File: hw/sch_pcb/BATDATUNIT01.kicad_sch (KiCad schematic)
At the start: 116 parts, among them IC1 MAX14502AETL+, J1 USBC_USB4105-GF-A, J22 HEADER_2x03, J4 46436-9327, J9 SD_Card-FPS009-4200-0, Q1 BC817-25, Q2 BC817-25, Q3 BC817-25, Q4 BC817-25, SW3 KMT031, SW3 SKRTLAE010, SW4 KMT031, SW4 SKRTLAE010, U10 ATMEGA1284P-AU, U11 PCF85263A, U11 TCA4307, U2 USBLC6-2SC6, U3 FT260Q-T, U4 PCA9541ABS/01, U6 AT24CS64-SSHM, U6 SHT35-DIS, U7 TMUX1574DYYR, Y1 19.2 MHz, Y1 8 MHz, Y2 ABS07-120-32.768KHZ-T

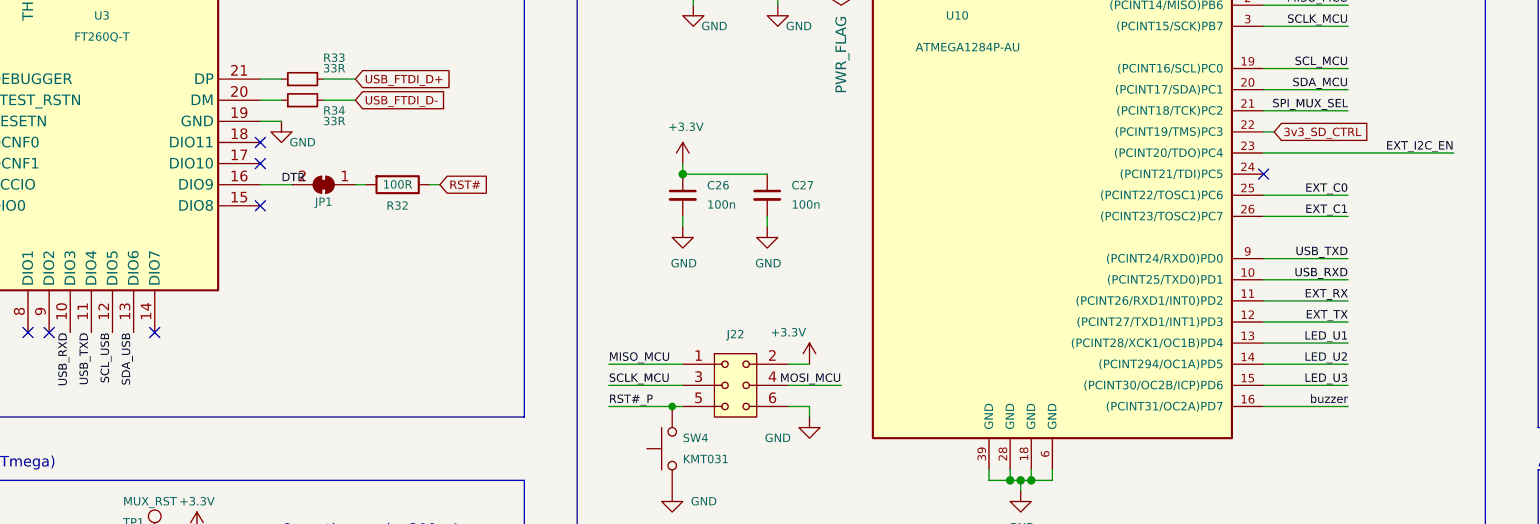
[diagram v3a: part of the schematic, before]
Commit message: add USB detect from FTDI to MCU
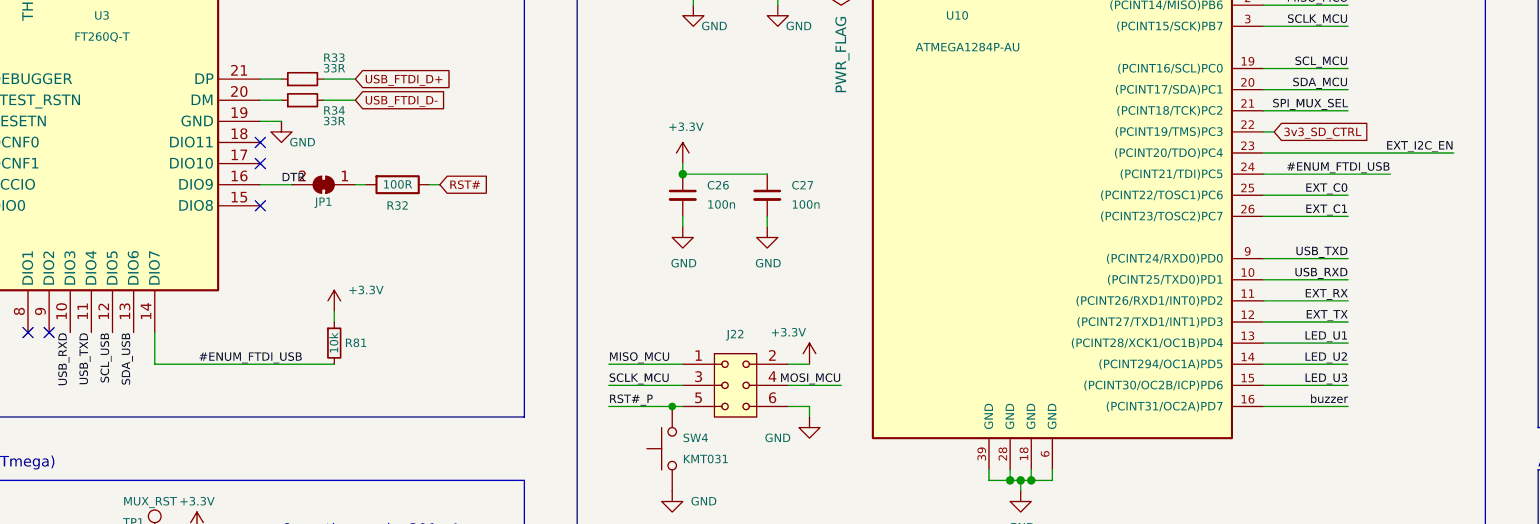
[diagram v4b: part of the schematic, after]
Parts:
- added R81: 10k, Resistor_SMD:R_0805_2012Metric, symbol Device:R_Small
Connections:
- net +3.3V: now also R81.1
- net #ENUM_FTDI_USB: now reaches U10.24 ((PCINT21/TDI)PC5)
- net #ENUM_FTDI_USB: now also U3.14 (DIO7), R81.2
- no-connect marks 38 -> 36
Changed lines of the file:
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@@
   (no_connect (at 151.13 243.84))
   (no_connect (at 355.6 196.85))
-  (no_connect (at 304.8 184.15))
   (no_connect (at 60.96 163.83))
   (no_connect (at 318.77 52.07))
   (no_connect (at 304.8 135.89))
   (no_connect (at 40.64 135.89))
-  (no_connect (at 171.45 203.2))
   (no_connect (at 378.46 68.58))
   (no_connect (at 151.13 254))
@@
     (stroke (width 0) (type default))
   )
+  (wire (pts (xy 304.8 184.15) (xy 320.04 184.15))
+    (stroke (width 0) (type default))
+  )
   (wire (pts (xy 109.22 49.53) (xy 109.22 48.26))
     (stroke (width 0) (type default))
@@
     (stroke (width 0) (type default))
   )
+  (wire (pts (xy 193.04 200.66) (xy 193.04 201.93))
+    (stroke (width 0) (type default))
+  )
   (wire (pts (xy 233.68 146.05) (xy 237.49 146.05))
     (stroke (width 0) (type default))
@@
     (stroke (width 0) (type default))
   )
+  (wire (pts (xy 171.45 207.01) (xy 193.04 207.01))
+    (stroke (width 0) (type default))
+  )
   (wire (pts (xy 368.3 232.41) (xy 368.3 233.68))
     (stroke (width 0) (type default))
@@
     (stroke (width 0) (type default))
   )
+  (wire (pts (xy 171.45 207.01) (xy 171.45 203.2))
+    (stroke (width 0) (type default))
+  )
   (wire (pts (xy 274.32 219.71) (xy 274.32 220.98))
     (stroke (width 0) (type solid))
@@
     (effects (font (size 1 1)) (justify left bottom))
   )
+  (label "#ENUM_FTDI_USB" (at 189.23 207.01 180) (fields_autoplaced)
+    (effects (font (size 1 1)) (justify right bottom))
+  )
   (label "RST#_P" (at 226.06 212.09 0) (fields_autoplaced)
     (effects (font (size 1 1)) (justify left bottom))
@@
     (effects (font (size 1 1)) (justify right bottom))
   )
+  (label "#ENUM_FTDI_USB" (at 320.04 184.15 180) (fields_autoplaced)
+    (effects (font (size 1 1)) (justify right bottom))
+  )
   (label "LED_U3" (at 128.27 104.14 0) (fields_autoplaced)
     (effects (font (size 1 1)) (justify left bottom))
@@
     )
   )
+  (symbol (lib_id "Device:R_Small") (at 193.04 204.47 0) (unit 1)
+    (in_bom yes) (on_board yes) (dnp no)
+    (property "Reference" "R81" (at 194.31 204.47 0)
+      (effects (font (size 1 1)) (justify left))
+    )
+    (property "Value" "10k" (at 193.04 205.74 90)
+      (effects (font (size 1 1)) (justify left))
+    )
+    (property "Footprint" "Resistor_SMD:R_0805_2012Metric" (at 193.04 204.47 0)
+      (effects (font (size 1 1)) hide)
+    )
+    (property "Datasheet" "~" (at 193.04 204.47 0)
+      (effects (font (size 1 1)) hide)
+    )
+    (property "UST_ID" "" (at 193.04 204.47 0)
+      (effects (font (size 1 1)) hide)
+    )
+    (pin "1")
+    (pin "2")
+    (instances
+      (project "BATDATUNIT01"
+        (path "/cca3030a-cb35-4155-89c2-3a41e5a0afad"
+          (reference "R81") (unit 1)
+        )
+      )
+    )
+  )
   (symbol (lib_id "Mechanical:Fiducial") (at 40.64 271.78 0) (unit 1)
     (in_bom no) (on_board yes) (dnp no) (fields_autoplaced)
@@
         )
       )
+    )
+  )
+  (symbol (lib_id "power:+3.3V") (at 193.04 200.66 0) (unit 1)
+    (in_bom yes) (on_board yes) (dnp no)
+    (property "Reference" "#PWR?" (at 193.04 204.47 0)
+      (effects (font (size 1 1)) hide)
+    )
+    (property "Value" "+3.3V" (at 196.85 198.12 0)
+      (effects (font (size 1 1)))
+    )
+    (property "Footprint" "" (at 193.04 200.66 0)
+      (effects (font (size 1 1)) hide)
+    )
+    (property "Datasheet" "" (at 193.04 200.66 0)
+      (effects (font (size 1 1)) hide)
+    )
+    (pin "1")
+    (instances
+      (project "Peripherals"
+        (path "/5251a3af-ca7f-447d-b796-a6d47f48d23f"
+          (reference "#PWR?") (unit 1)
+        )
+      )
+      (project "BATDATUNIT01"
+        (path "/cca3030a-cb35-4155-89c2-3a41e5a0afad"
+          (reference "#PWR01") (unit 1)
+        )
+      )
+      (project "DATALOGGER02"
+        (path "/d5fa3405-b56f-43e6-a8bd-3ff789d79996/8c16a5bf-8019-4e77-9247-0011396b8bad"
+          (reference "#PWR?") (unit 1)
+        )
+      )

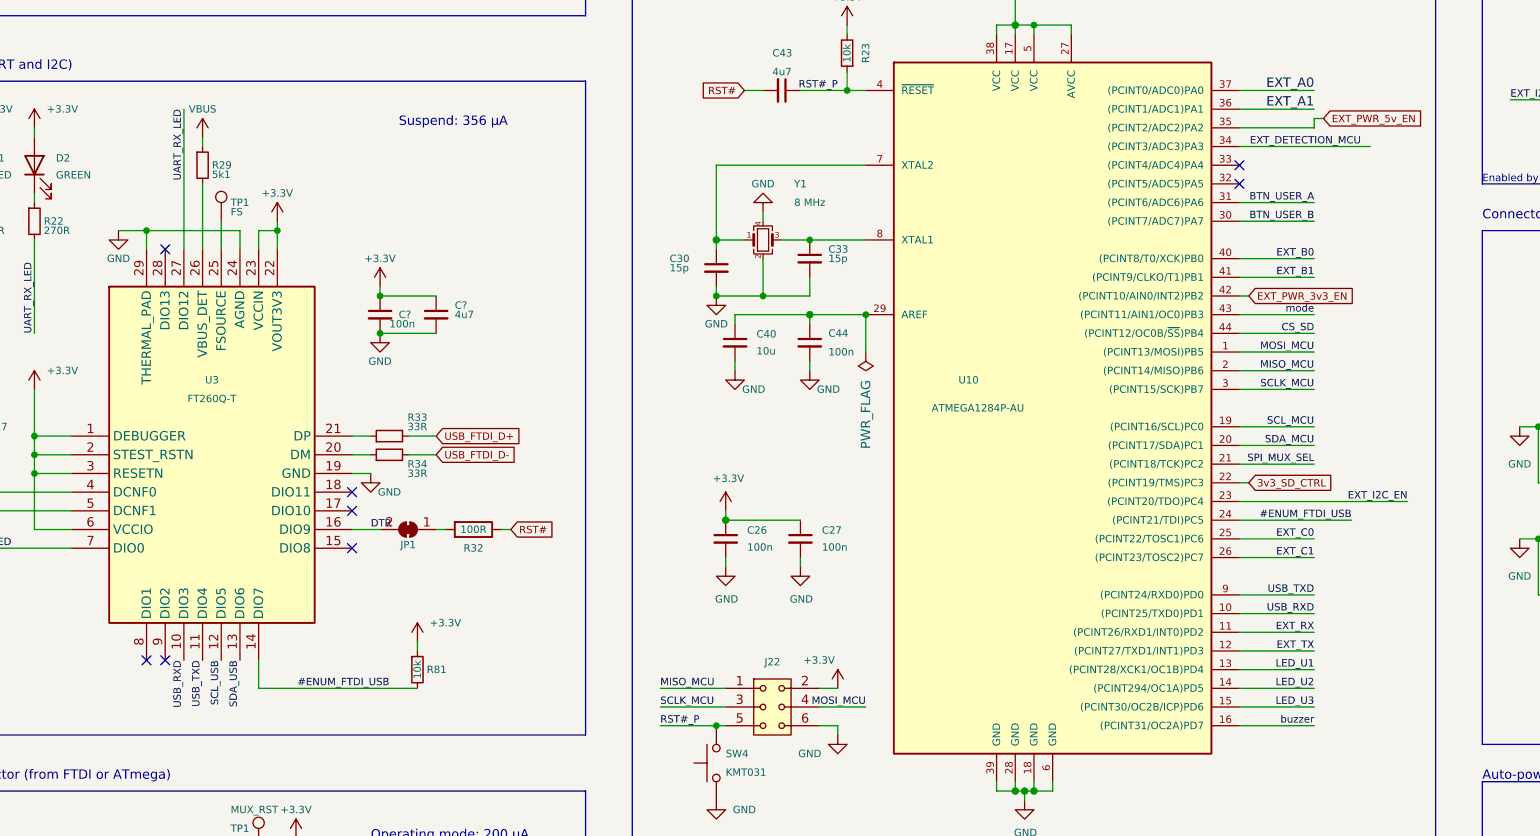
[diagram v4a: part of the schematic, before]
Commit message: add RTS, CTS
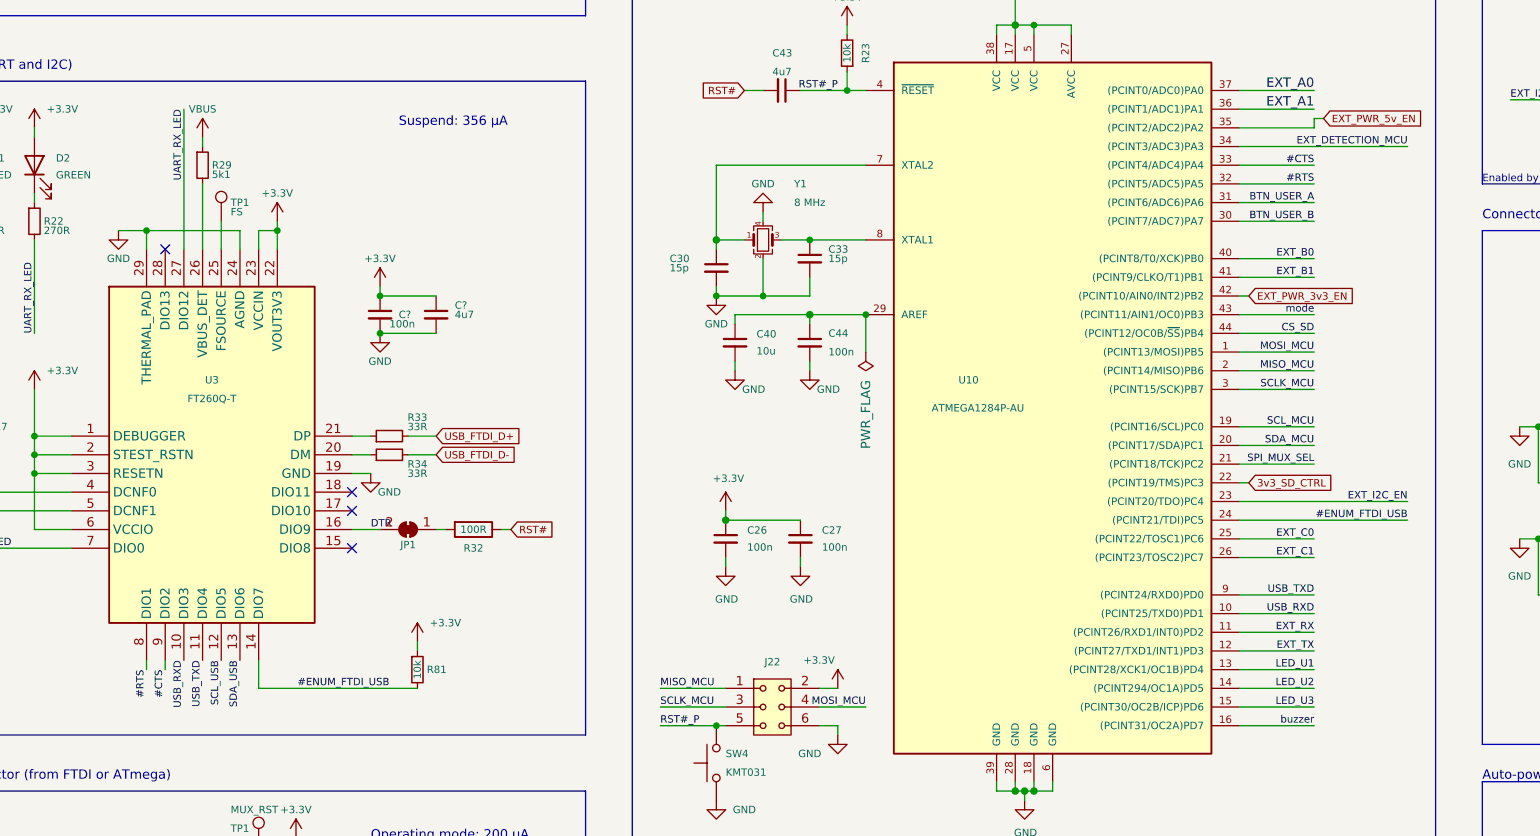
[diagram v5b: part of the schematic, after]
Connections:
- net #RTS: now reaches U10.32 ((PCINT5/ADC5)PA5)
- net #RTS: now also U3.8 (DIO1)
- net #CTS: now reaches U10.33 ((PCINT4/ADC4)PA4)
- net #CTS: now also U3.9 (DIO2)
- no-connect marks 36 -> 32
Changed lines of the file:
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@@
   (no_connect (at 81.28 120.65))
   (no_connect (at 388.62 181.61))
-  (no_connect (at 158.75 203.2))
-  (no_connect (at 156.21 203.2))
   (no_connect (at 58.42 163.83))
   (no_connect (at 184.15 187.96))
@@
   (no_connect (at 60.96 163.83))
   (no_connect (at 318.77 52.07))
-  (no_connect (at 304.8 135.89))
   (no_connect (at 40.64 135.89))
   (no_connect (at 378.46 68.58))
@@
   (no_connect (at 45.72 58.42))
   (no_connect (at 271.78 266.7))
-  (no_connect (at 304.8 138.43))
   (no_connect (at 254 52.07))
   (no_connect (at 45.72 60.96))
@@
     (stroke (width 0) (type solid))
   )
+  (wire (pts (xy 304.8 133.35) (xy 327.66 133.35))
+    (stroke (width 0) (type default))
+  )
   (wire (pts (xy 87.63 143.51) (xy 81.28 143.51))
     (stroke (width 0) (type default))
@@
     (stroke (width 0) (type default))
   )
-  (wire (pts (xy 304.8 133.35) (xy 322.58 133.35))
-    (stroke (width 0) (type default))
-  )
   (wire (pts (xy 387.35 113.03) (xy 389.89 113.03))
     (stroke (width 0) (type default))
@@
     (stroke (width 0) (type default))
   )
+  (wire (pts (xy 314.96 138.43) (xy 304.8 138.43))
+    (stroke (width 0) (type default))
+  )
+  (wire (pts (xy 158.75 203.2) (xy 158.75 204.47))
+    (stroke (width 0) (type default))
+  )
   (wire (pts (xy 140.97 175.26) (xy 140.97 177.8))
     (stroke (width 0) (type default))
@@
     (stroke (width 0) (type default))
   )
-  (wire (pts (xy 304.8 184.15) (xy 320.04 184.15))
+  (wire (pts (xy 304.8 184.15) (xy 327.66 184.15))
     (stroke (width 0) (type default))
   )
@@
     (stroke (width 0) (type default))
   )
+  (wire (pts (xy 314.96 135.89) (xy 304.8 135.89))
+    (stroke (width 0) (type default))
+  )
   (wire (pts (xy 359.41 38.1) (xy 359.41 39.37))
     (stroke (width 0) (type default))
@@
   (wire (pts (xy 275.59 220.98) (xy 276.86 220.98))
     (stroke (width 0) (type solid))
+  )
+  (wire (pts (xy 156.21 203.2) (xy 156.21 204.47))
+    (stroke (width 0) (type default))
   )
   (wire (pts (xy 27.94 220.98) (xy 29.21 220.98))
@@
     (effects (font (size 1 1)) (justify right bottom))
   )
+  (label "#CTS" (at 158.75 204.47 270) (fields_autoplaced)
+    (effects (font (size 1 1)) (justify right bottom))
+  )
   (label "SCL_USB" (at 166.37 203.2 270) (fields_autoplaced)
     (effects (font (size 1 1)) (justify right bottom))
@@
     (effects (font (size 1 1)) (justify right bottom))
   )
-  (label "#ENUM_FTDI_USB" (at 320.04 184.15 180) (fields_autoplaced)
+  (label "#ENUM_FTDI_USB" (at 327.66 184.15 180) (fields_autoplaced)
+    (effects (font (size 1 1)) (justify right bottom))
+  )
+  (label "#RTS" (at 314.96 138.43 180) (fields_autoplaced)
     (effects (font (size 1 1)) (justify right bottom))
   )
@@
     (effects (font (size 1 1)) (justify left bottom))
   )
+  (label "#CTS" (at 314.96 135.89 180) (fields_autoplaced)
+    (effects (font (size 1 1)) (justify right bottom))
+  )
   (label "EXT_DETECTION_MCU" (at 386.08 233.68 180) (fields_autoplaced)
     (effects (font (size 1 1)) (justify right bottom))
@@
     (effects (font (size 1 1)) (justify right bottom))
   )
-  (label "EXT_DETECTION_MCU" (at 321.31 133.35 180) (fields_autoplaced)
+  (label "EXT_DETECTION_MCU" (at 327.66 133.35 180) (fields_autoplaced)
     (effects (font (size 1 1)) (justify right bottom))
   )
@@
     (effects (font (size 1 1)) (justify right bottom))
   )
+  (label "#RTS" (at 156.21 204.47 270) (fields_autoplaced)
+    (effects (font (size 1 1)) (justify right bottom))
+  )

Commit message: Resolve majority of DRC issues.
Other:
- moved on the sheet: R81
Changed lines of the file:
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@@
     (stroke (width 0) (type default))
   )
-  (wire (pts (xy 193.04 200.66) (xy 193.04 201.93))
+  (wire (pts (xy 194.31 199.39) (xy 194.31 200.66))
     (stroke (width 0) (type default))
   )
@@
     (stroke (width 0) (type default))
   )
-  (wire (pts (xy 171.45 207.01) (xy 193.04 207.01))
+  (wire (pts (xy 171.45 207.01) (xy 194.31 207.01))
     (stroke (width 0) (type default))
   )
@@
     (stroke (width 0) (type solid))
   )
+  (wire (pts (xy 194.31 207.01) (xy 194.31 205.74))
+    (stroke (width 0) (type default))
+  )
   (wire (pts (xy 177.8 35.56) (xy 177.8 38.1))
     (stroke (width 0) (type default))
@@
     )
   )
-  (symbol (lib_id "Device:R_Small") (at 193.04 204.47 0) (unit 1)
+  (symbol (lib_id "Device:R_Small") (at 194.31 203.2 0) (unit 1)
     (in_bom yes) (on_board yes) (dnp no)
-    (property "Reference" "R81" (at 194.31 204.47 0)
+    (property "Reference" "R81" (at 195.58 203.2 0)
       (effects (font (size 1 1)) (justify left))
     )
-    (property "Value" "10k" (at 193.04 205.74 90)
+    (property "Value" "10k" (at 194.31 204.47 90)
       (effects (font (size 1 1)) (justify left))
     )
-    (property "Footprint" "Resistor_SMD:R_0805_2012Metric" (at 193.04 204.47 0)
+    (property "Footprint" "Resistor_SMD:R_0805_2012Metric" (at 194.31 203.2 0)
       (effects (font (size 1 1)) hide)
     )
-    (property "Datasheet" "~" (at 193.04 204.47 0)
+    (property "Datasheet" "~" (at 194.31 203.2 0)
       (effects (font (size 1 1)) hide)
     )
-    (property "UST_ID" "" (at 193.04 204.47 0)
+    (property "UST_ID" "" (at 194.31 203.2 0)
       (effects (font (size 1 1)) hide)
     )
@@
     )
   )
-  (symbol (lib_id "power:+3.3V") (at 193.04 200.66 0) (unit 1)
+  (symbol (lib_id "power:+3.3V") (at 194.31 199.39 0) (unit 1)
     (in_bom yes) (on_board yes) (dnp no)
-    (property "Reference" "#PWR?" (at 193.04 204.47 0)
+    (property "Reference" "#PWR?" (at 194.31 203.2 0)
       (effects (font (size 1 1)) hide)
     )
-    (property "Value" "+3.3V" (at 196.85 198.12 0)
+    (property "Value" "+3.3V" (at 198.12 196.85 0)
       (effects (font (size 1 1)))
     )
-    (property "Footprint" "" (at 193.04 200.66 0)
+    (property "Footprint" "" (at 194.31 199.39 0)
       (effects (font (size 1 1)) hide)
     )
-    (property "Datasheet" "" (at 193.04 200.66 0)
+    (property "Datasheet" "" (at 194.31 199.39 0)
       (effects (font (size 1 1)) hide)
     )

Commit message: Change oscillator footprint. WIP
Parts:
- Y1: footprint Crystal:Crystal_SMD_2016-4Pin_2.0x1.6mm -> Crystal:Crystal_SMD_2520-4Pin_2.5x2.0mm
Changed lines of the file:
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@@
       (effects (font (size 1.27 1.27)))
     )
-    (property "Footprint" "Crystal:Crystal_SMD_2016-4Pin_2.0x1.6mm" (at 104.14 198.12 0)
+    (property "Footprint" "Crystal:Crystal_SMD_2520-4Pin_2.5x2.0mm" (at 104.14 198.12 0)
       (effects (font (size 1.27 1.27)) hide)
     )
